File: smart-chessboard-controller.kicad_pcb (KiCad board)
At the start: 4 copper layers, 89.8 x 50.9 mm, 61 parts, among them J1 USB_C_Receptacle_USB2.0, J2 Micro_SD_Card_Det_Hirose_DM3C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, J3 Conn_02x03_Odd_Even, J4 Conn_01x12_MountingPin, J5 NX3224T024, J8 Conn_01x05, J9 Conn_01x05, Q1 S8050, Q2 S8050, SW2 SW_SPST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

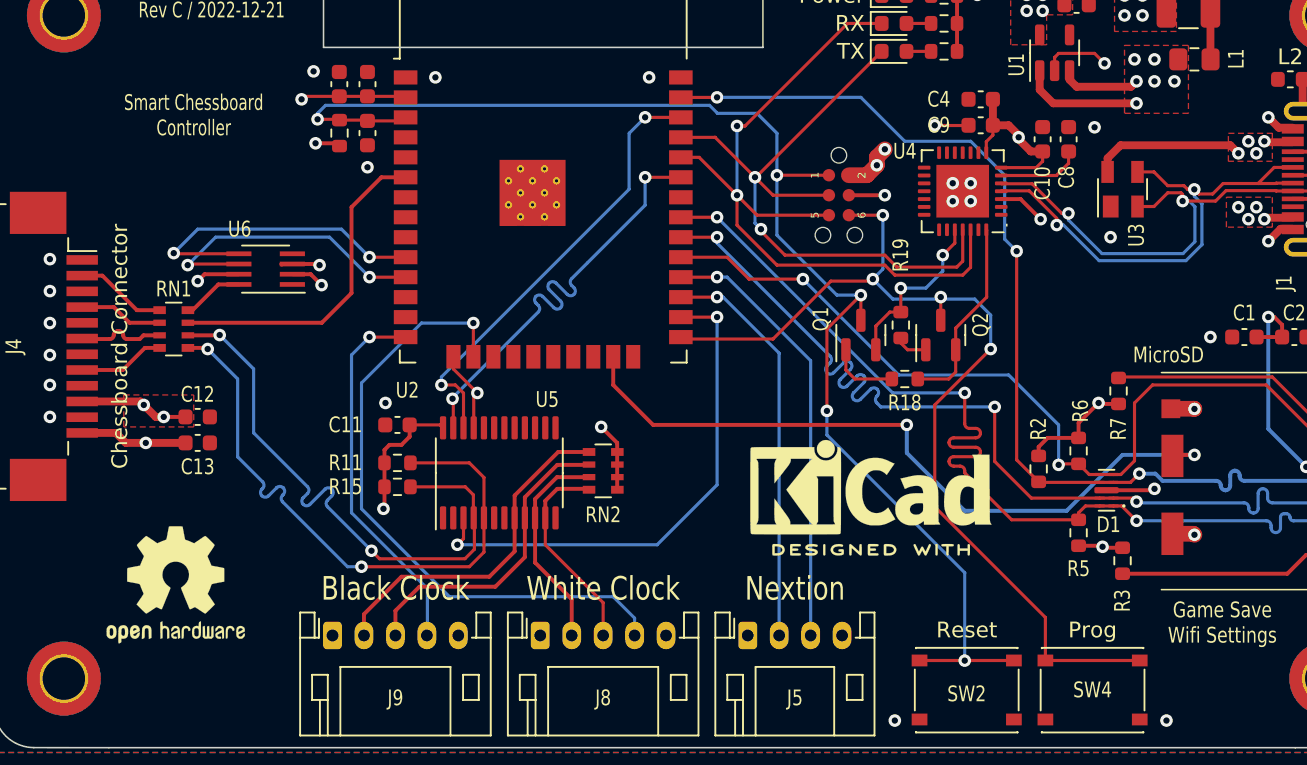
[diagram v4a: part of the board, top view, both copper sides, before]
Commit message: add bypass caps
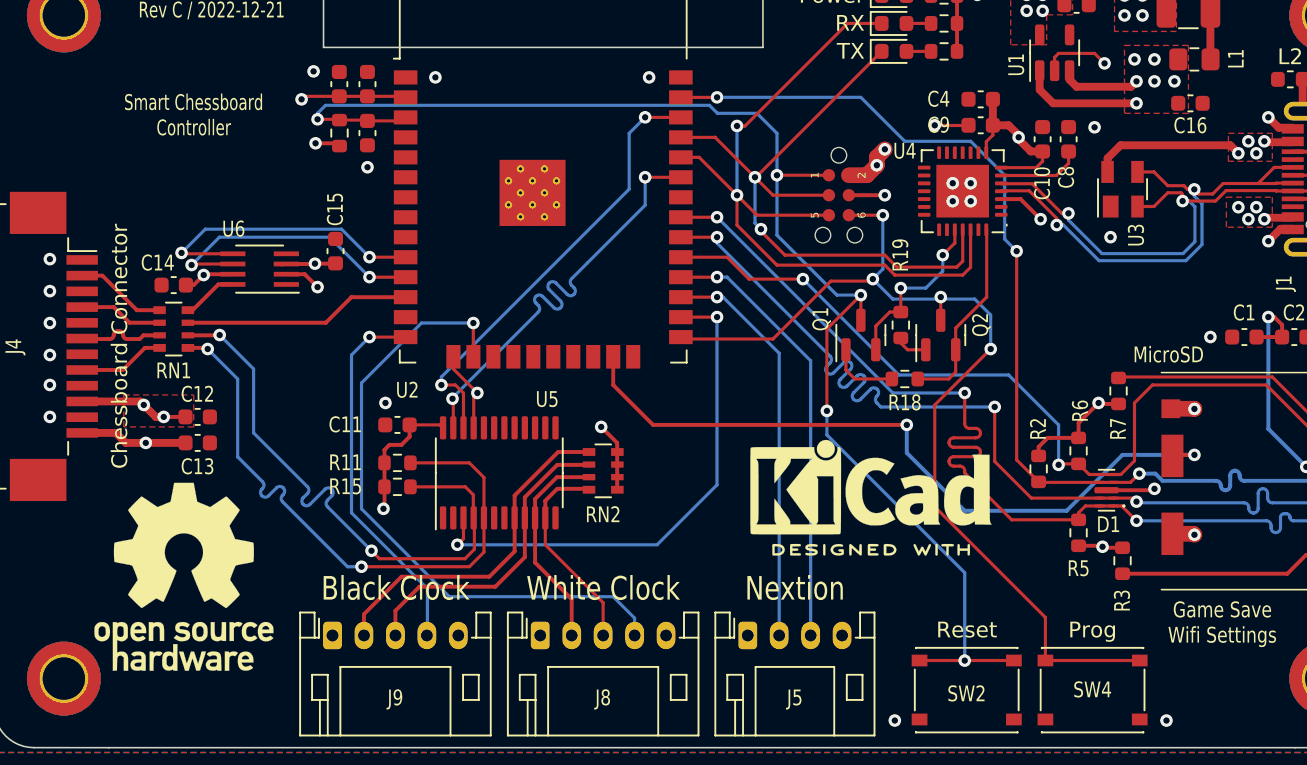
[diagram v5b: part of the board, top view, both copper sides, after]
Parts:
- added C14: 100nF, Capacitor_SMD:C_0603_1608Metric, F.Cu at (85.2, 74.8)
- added C15: 100nF, Capacitor_SMD:C_0603_1608Metric, F.Cu at (95.5, 72.6)
- added C16: 22uF, Capacitor_SMD:C_0603_1608Metric, F.Cu at (149.9, 63.2)
- REF**: value OSHW-Logo2_9.8x8mm_SilkScreen -> OSHW-Logo_11.4x12mm_SilkScreen; footprint Symbol:OSHW-Logo2_9.8x8mm_SilkScreen -> Symbol:OSHW-Logo_11.4x12mm_SilkScreen
- RN1: value 33 -> 0
- moved REF** 0.72 mm to (85.9, 93.3)
- moved U6 0.38 mm to (90.7, 73.8)
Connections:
- J4 pad MP: unconnected-(J4-PadMP) -> GND
- U2 pad 12: unconnected-(U2-Pad12) -> /IO_INT
- U2 pad 6: /IO_INT -> unconnected-(U2-Pad6)
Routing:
- net /IO_INT: track 20.9 -> 14.5 mm
- net /LED_IC_3: track 20.3 -> 18.9 mm
- net 3V3: track 303.2 -> 304.3 mm
- net 5V: track 136.5 -> 137.5 mm
- net /VLS_EN: track 18.9 -> 18.0 mm

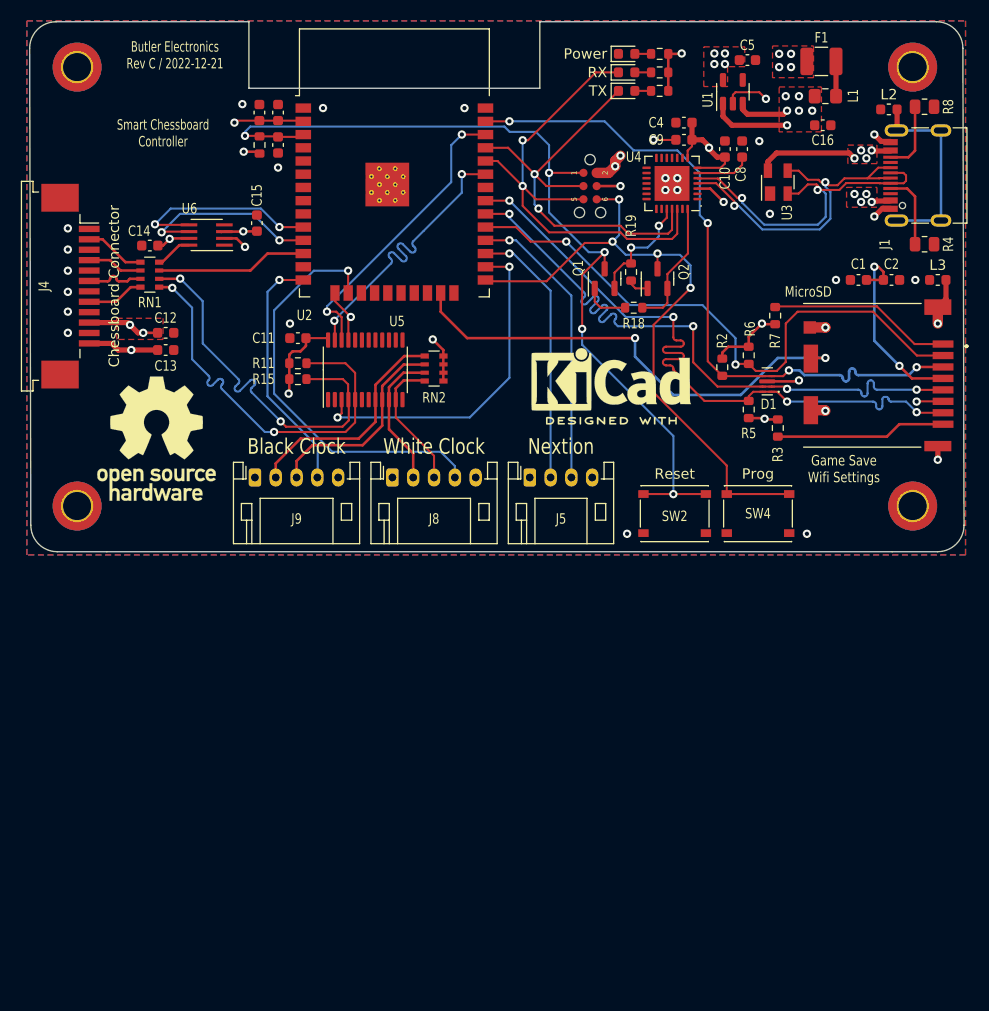
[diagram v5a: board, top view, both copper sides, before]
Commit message: update design to use ESP32 WROVER module
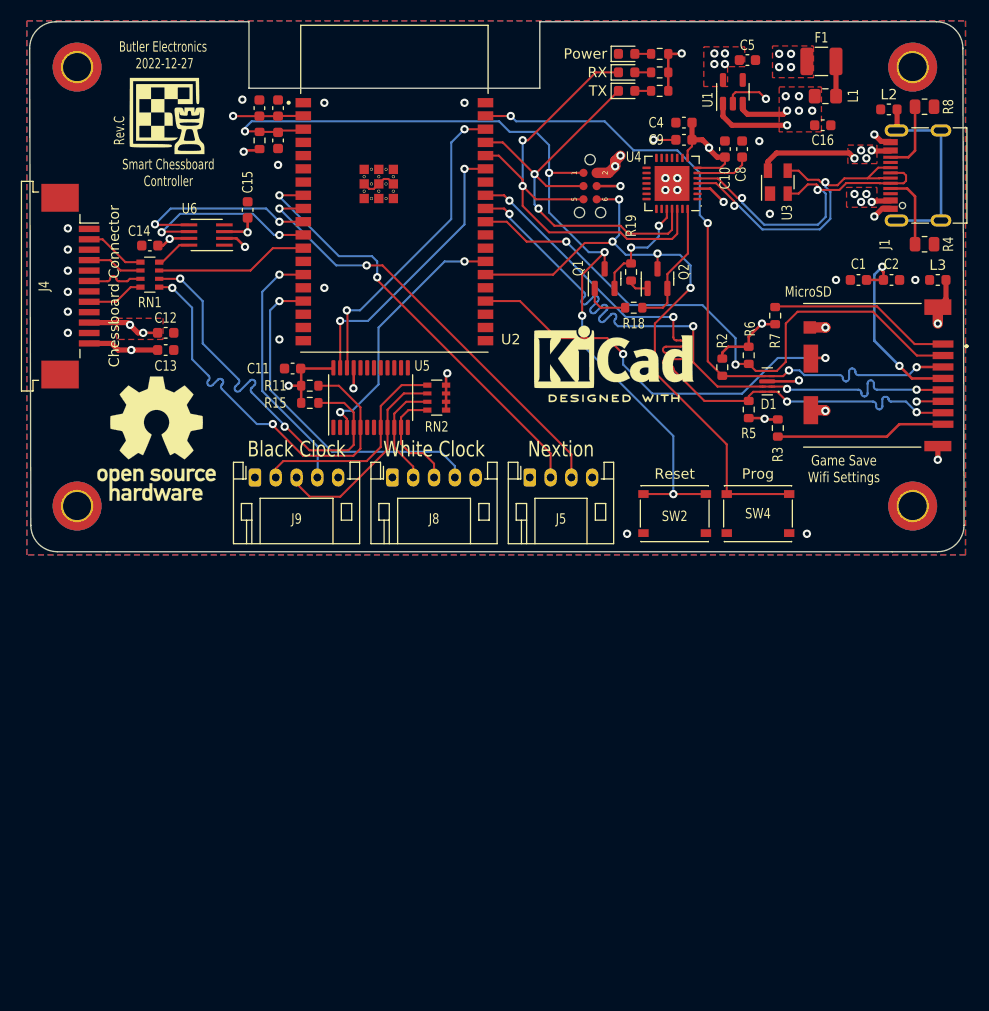
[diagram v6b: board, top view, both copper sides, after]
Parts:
- added G***: LOGO, User Custom Footprint:chess-logo, F.Cu at (86.6, 62.0)
- U2: value ESP32-WROOM-32E (8MB) -> ESP32-WROVER-32E; footprint RF_Module:ESP32-WROOM-32 -> User Custom Footprint:XCVR_ESP32-WROVER-E-N4R8
- moved C11 2.96 mm to (98.9, 86.6)
- moved RN2 2.81 mm to (112.8, 89.4)
- moved U5 2.72 mm to (106.4, 89.4)
- moved R15 2.56 mm to (100.6, 89.9)
- moved R11 2.44 mm to (100.6, 88.3)
- moved REF** 2.17 mm to (129.8, 85.5)
- moved C15 1.55 mm to (94.6, 71.4)
- moved U2 0.51 mm to (108.7, 69.3)
- moved C3 0.43 mm to (97.5, 64.7)
- moved C6 0.43 mm to (97.5, 61.6)
- moved C7 0.43 mm to (95.7, 61.6)
- moved R1 0.43 mm to (95.8, 64.7)
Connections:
- U2 pad 27: /RX2 -> unconnected-(U2-Pad27)
- U2 pad 28: /TX2 -> unconnected-(U2-Pad28)
- U2 pad 8: unconnected-(U2-Pad8) -> /RX2
- U2 pad 9: unconnected-(U2-Pad9) -> /TX2
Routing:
- net /RX2: track 25.7 -> 42.1 mm, vias 1 -> 2
- net /TX2: track 27.9 -> 42.4 mm, vias 1 -> 2
- net /~{I2C_RESET}: track 32.9 -> 24.9 mm
- net /W_MOVE: track 39.7 -> 33.1 mm
- net /SD_DET: track 46.0 -> 39.8 mm
- net /SDA_DWC: track 13.6 -> 10.5 mm
- net /SCL_DWC: track 13.2 -> 10.6 mm
- net 3V3: track 304.3 -> 302.3 mm
- net /~{I2C_SCL}: track 28.5 -> 30.4 mm
- net /SDA_DBC: track 22.0 -> 20.5 mm
- net /B_MOVE: track 23.8 -> 24.7 mm
- net /~{I2C_SDA}: track 28.4 -> 27.6 mm
- net /ESP_RX: track 47.9 -> 48.5 mm
- net GND: track 28.8 -> 29.1 mm, vias 31 -> 32
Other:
- board text added: "${COMPANY} ${ISSUE_DATE}"
- board text added: "Rev.${REVISION}"
- board text removed: "${COMPANY} Rev ${REVISION} / ${ISSUE_DATE}"
